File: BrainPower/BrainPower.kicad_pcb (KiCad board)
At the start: 2 copper layers, 149.9 x 111.3 mm, 10 parts, among them J1 BarrelJack_Horizontal, J2 PhoenixContact_MCV_1,5_2-G-5.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, P1 Golden finger, PCIeX1, Dual, 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

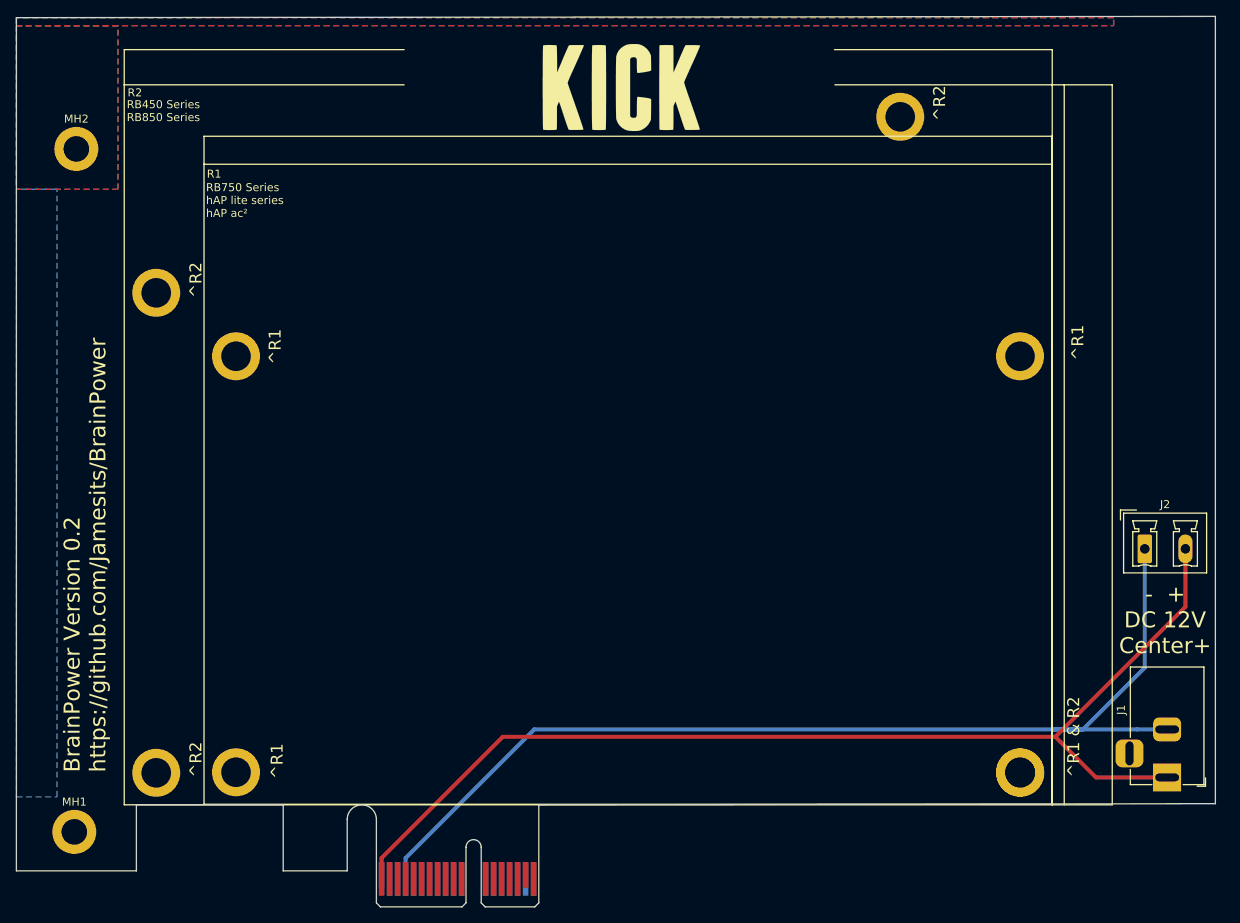
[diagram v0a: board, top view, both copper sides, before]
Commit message: fix footprint positioning
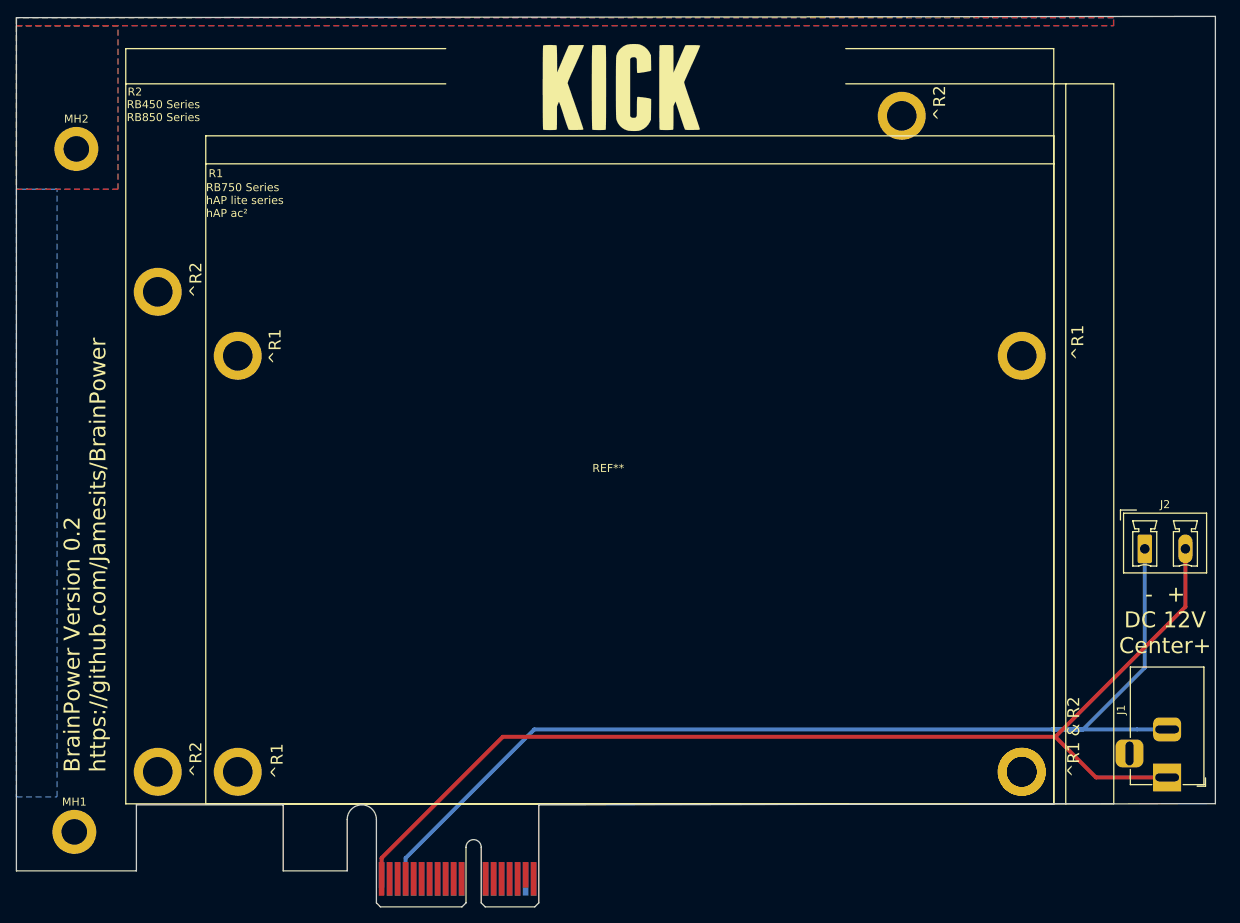
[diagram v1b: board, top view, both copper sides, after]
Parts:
- moved R2 77.2 mm to (87.0, 53.0)
- moved R1 0.22 mm to (150.0, 113.0)
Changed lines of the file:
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@@
   )
   (module Footprints:RB450Gx4 (layer F.Cu)
-    (at 147.18538 101.3714)
-    (fp_text reference R2 (at -59.04738 -47.2694 180) (layer F.SilkS)
-      (effects (font (size 1 1) (thickness 0.15)))
-    )
-    (fp_text value RB450Gx4 (at -0.0635 0.8048 180) (layer F.Fab)
-      (effects (font (size 1 1) (thickness 0.15)))
-    )
-    (fp_text user LED (at 59.9313 -11.049 -90) (layer Dwgs.User)
-      (effects (font (size 1 1) (thickness 0.15)))
-    )
-    (fp_text user "DC Jack" (at 59.9313 13.0175 -90) (layer Dwgs.User)
-      (effects (font (size 1 1) (thickness 0.15)))
-    )
-    (fp_text user "Serial Port" (at 60.0456 -37.1094 -90) (layer Dwgs.User)
-      (effects (font (size 1 1) (thickness 0.15)))
-    )
-    (fp_text user "RJ45 Ports" (at -0.0762 -50.4317 180) (layer Dwgs.User)
-      (effects (font (size 1 1) (thickness 0.15)))
-    )
-    (fp_line (start 57.1242 41.7527) (end 57.1242 -48.2473) (layer F.SilkS) (width 0.12))
-    (fp_line (start 63.1242 -48.2473) (end 55.6242 -48.2473) (layer F.SilkS) (width 0.12))
-    (fp_line (start 63.1242 41.7527) (end 63.1242 -48.2473) (layer F.SilkS) (width 0.12))
-    (fp_line (start 55.6242 41.7527) (end 63.1242 41.7527) (layer F.SilkS) (width 0.12))
-    (fp_line (start 55.6242 -52.6473) (end 55.6242 -48.2473) (layer F.SilkS) (width 0.12))
-    (fp_line (start 28.3972 -52.6415) (end 55.6242 -52.6473) (layer F.SilkS) (width 0.12))
-    (fp_line (start -60.3758 -48.2473) (end -60.3758 -52.6473) (layer F.SilkS) (width 0.12))
-    (fp_line (start 55.6242 -48.2473) (end 28.448 -48.2473) (layer F.SilkS) (width 0.12))
-    (fp_line (start 55.6242 41.7527) (end 55.6242 -48.2473) (layer F.SilkS) (width 0.12))
-    (fp_line (start -60.3758 41.7527) (end 55.6242 41.7527) (layer F.SilkS) (width 0.12))
-    (fp_line (start -60.3758 -48.2473) (end -60.3758 41.7527) (layer F.SilkS) (width 0.12))
-    (fp_line (start -60.3758 -52.6473) (end -25.3873 -52.6415) (layer F.SilkS) (width 0.12))
-    (fp_line (start -25.3873 -48.2473) (end -60.3758 -48.2473) (layer F.SilkS) (width 0.12))
-    (pad 3 thru_hole circle (at -56.3758 37.7527 180) (size 6 6) (drill 3.7) (layers *.Cu *.Mask))
-    (pad 4 thru_hole circle (at 51.6242 37.7527 180) (size 6 6) (drill 3.7) (layers *.Cu *.Mask))
-    (pad 1 thru_hole circle (at -56.3758 -22.2473 180) (size 6 6) (drill 3.7) (layers *.Cu *.Mask))
-    (pad 2 thru_hole circle (at 36.6242 -44.2473 180) (size 6 6) (drill 3.7) (layers *.Cu *.Mask))
+    (at 87 53)
+    (fp_text reference R2 (at 1.138 1 180) (layer F.SilkS)
+      (effects (font (size 1 1) (thickness 0.15)))
+    )
+    (fp_text value RB450Gx4 (at 60 51 180) (layer F.Fab) hide
+      (effects (font (size 1 1) (thickness 0.15)))
+    )
+    (fp_text user "DC Jack" (at 120 58 -90) (layer Dwgs.User)
+      (effects (font (size 1 1) (thickness 0.15)))
+    )
+    (fp_text user REF** (at 60.3115 48.05218 180) (layer F.SilkS)
+      (effects (font (size 1 1) (thickness 0.15)))
+    )
+    (fp_text user "RJ45 Ports" (at 18 -2 180) (layer Dwgs.User)
+      (effects (font (size 1 1) (thickness 0.15)))
+    )
+    (fp_text user LED (at 120 41 -90) (layer Dwgs.User)
+      (effects (font (size 1 1) (thickness 0.15)))
+    )
+    (fp_text user RB450Gx4 (at 60.3115 49.05218 180) (layer F.Fab)
+      (effects (font (size 1 1) (thickness 0.15)))
+    )
+    (fp_text user "Serial Port" (at 120 18 -90) (layer Dwgs.User)
+      (effects (font (size 1 1) (thickness 0.15)))
+    )
+    (fp_line (start 0 0) (end 0 90) (layer F.SilkS) (width 0.12))
+    (fp_line (start 116 90) (end 116 0) (layer F.SilkS) (width 0.12))
+    (fp_line (start 116 0) (end 90 0) (layer F.SilkS) (width 0.12))
+    (fp_line (start 123.5 90) (end 123.5 0) (layer F.SilkS) (width 0.12))
+    (fp_line (start 90 -4.4) (end 116 -4.4) (layer F.SilkS) (width 0.12))
+    (fp_line (start 123.5 0) (end 116 0) (layer F.SilkS) (width 0.12))
+    (fp_line (start 0 90) (end 116 90) (layer F.SilkS) (width 0.12))
+    (fp_line (start 0 0) (end 0 -4.4) (layer F.SilkS) (width 0.12))
+    (fp_line (start 116 90) (end 123.5 90) (layer F.SilkS) (width 0.12))
+    (fp_line (start 117.5 90) (end 117.5 0) (layer F.SilkS) (width 0.12))
+    (fp_line (start 116 -4.4) (end 116 0) (layer F.SilkS) (width 0.12))
+    (fp_line (start 40 0) (end 0 0) (layer F.SilkS) (width 0.12))
+    (fp_line (start 0 -4.4) (end 40 -4.4) (layer F.SilkS) (width 0.12))
+    (pad 2 thru_hole circle (at 97 4 180) (size 6 6) (drill 3.7) (layers *.Cu *.Mask))
+    (pad 1 thru_hole circle (at 4 26 180) (size 6 6) (drill 3.7) (layers *.Cu *.Mask))
+    (pad 4 thru_hole circle (at 112 86 180) (size 6 6) (drill 3.7) (layers *.Cu *.Mask))
+    (pad 3 thru_hole circle (at 4 86 180) (size 6 6) (drill 3.7) (layers *.Cu *.Mask))
   )
   (module Connector_Phoenix_MC_HighVoltage:PhoenixContact_MCV_1,5_2-G-5.08_1x02_P5.08mm_Vertical (layer F.Cu)
@@
   )
   (module Footprints:RB750Gr3 (layer F.Cu)
-    (at 149.7838 113.0554)
+    (at 150 113)
     (fp_text reference R1 (at -51.7398 -48.7934) (layer F.SilkS)
       (effects (font (size 1 1) (thickness 0.15)))
